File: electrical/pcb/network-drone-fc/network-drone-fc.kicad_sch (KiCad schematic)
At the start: 78 parts, among them J1 U.FL-R-SMT-1, J2 TYPE-C 16PIN 2MD, J3 U.FL GPS, J4 ESC, J5 I2C port, J7 Charging board, U1 ESP32-S3FN8, U2 USBLC6-2SC6, U3 AP63205WU-7, U4 TLV75733PDBVR, U5 TPS7A2033PDBVR, U6 ICM-42688-P, U7 BMP581, U8 MAX-M10S, X1 Q22FA12800101

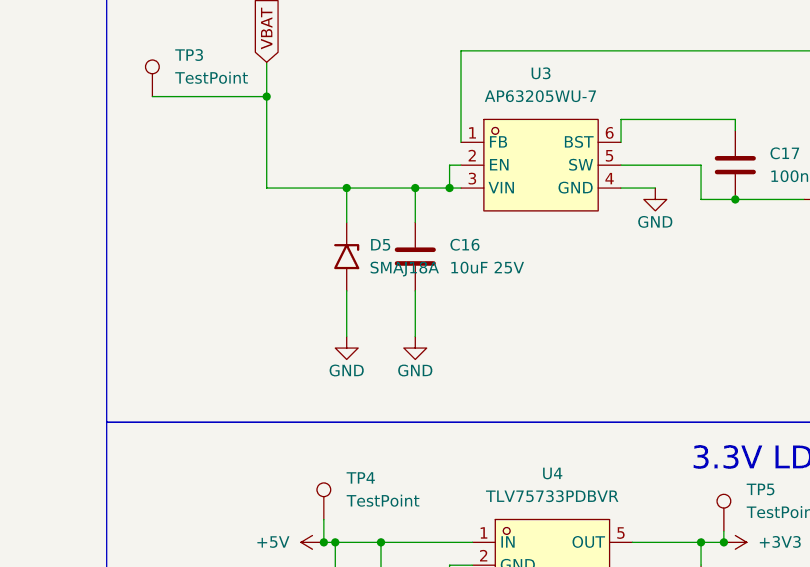
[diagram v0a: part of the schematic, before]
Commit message: Schematic: C35, 100 uF 25 V polymer tantalum bulk capacitor on VBAT
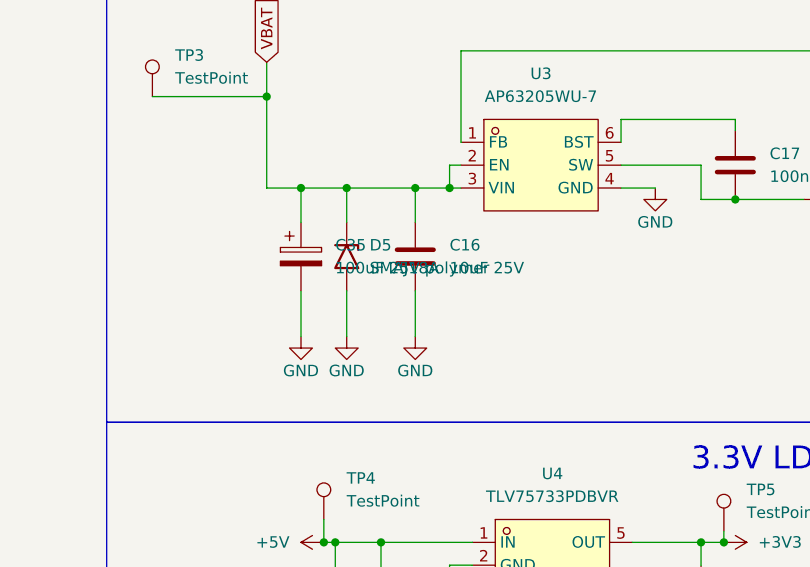
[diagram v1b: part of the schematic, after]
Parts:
- added C35: 100uF 25V polymer, Capacitor_Tantalum_SMD:CP_EIA-7343-31_Kemet-D_HandSolder, symbol Device:C_Polarized
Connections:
- net GND: now also C35.2
- net VBAT: now also C35.1
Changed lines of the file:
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@@
 	(wire
 		(pts
+			(xy 124.46 39.37) (xy 124.46 43.18)
+		)
+		(stroke
+			(width 0)
+			(type default)
+		)
+	)
+	(wire
+		(pts
+			(xy 124.46 50.8) (xy 124.46 55.88)
+		)
+		(stroke
+			(width 0)
+			(type default)
+		)
+	)
+	(junction
+		(at 124.46 39.37)
+		(diameter 0)
+		(color 0 0 0 0)
+	)
+	(wire
+		(pts
 			(xy 278.13 128.27) (xy 280.67 128.27)
 		)
@@
 	(symbol
 		(lib_id "power:GND")
+		(at 124.46 55.88 0)
+		(unit 1)
+		(exclude_from_sim no)
+		(in_bom yes)
+		(on_board yes)
+		(dnp no)
+		(fields_autoplaced yes)
+		(property "Reference" "#PWR0135"
+			(at 124.46 62.23 0)
+			(effects
+				(font
+					(size 1.27 1.27)
+				)
+				(hide yes)
+			)
+		)
+		(property "Value" "GND"
+			(at 124.46 59.69 0)
+			(effects
+				(font
+					(size 1.27 1.27)
+				)
+			)
+		)
+		(property "Footprint" ""
+			(at 124.46 55.88 0)
+			(effects
+				(font
+					(size 1.27 1.27)
+				)
+				(hide yes)
+			)
+		)
+		(property "Datasheet" ""
+			(at 124.46 55.88 0)
+			(effects
+				(font
+					(size 1.27 1.27)
+				)
+				(hide yes)
+			)
+		)
+		(property "Description" "Power symbol creates a global label with name \"GND\" , ground"
+			(at 124.46 55.88 0)
+			(effects
+				(font
+					(size 1.27 1.27)
+				)
+				(hide yes)
+			)
+		)
+		(pin "1"
+		)
+		(instances
+			(project "network-drone-fc"
+				(path "/f9d16c76-ade1-4aab-9e3b-738e650d90d6"
+					(reference "#PWR0135")
+					(unit 1)
+				)
+			)
+		)
+	)
+	(symbol
+		(lib_id "power:GND")
 		(at 191.77 58.42 0)
 		(unit 1)
@@
 					(unit 1)
 				)
+			)
+		)
+	)
+	(symbol
+		(lib_id "Device:C_Polarized")
+		(at 124.46 46.99 0)
+		(unit 1)
+		(exclude_from_sim no)
+		(in_bom yes)
+		(on_board yes)
+		(dnp no)
+		(fields_autoplaced yes)
+		(property "Reference" "C35"
+			(at 128.27 45.7199 0)
+			(effects
+				(font
+					(size 1.27 1.27)
+				)
+				(justify left)
+			)
+		)
+		(property "Value" "100uF 25V polymer"
+			(at 128.27 48.2599 0)
+			(effects
+				(font
+					(size 1.27 1.27)
+				)
+				(justify left)
+			)
+		)
+		(property "Footprint" "Capacitor_Tantalum_SMD:CP_EIA-7343-31_Kemet-D_HandSolder"
+			(at 125.425 50.8 0)
+			(effects
+				(font
+					(size 1.27 1.27)
+				)
+				(hide yes)
+			)
+		)
+		(property "Datasheet" "~"
+			(at 124.46 46.99 0)
+			(effects
+				(font
+					(size 1.27 1.27)
+				)
+				(hide yes)
+			)
+		)
+		(property "Description" "Polarized capacitor, Kyocera AVX TCJD107M025R0055E, LCSC C2159920"
+			(at 124.46 46.99 0)
+			(effects
+				(font
+					(size 1.27 1.27)
+				)
+				(hide yes)
+			)
+		)
+		(pin "2"
+		)
+		(pin "1"
+		)
+		(instances
+			(project "network-drone-fc"
+				(path "/f9d16c76-ade1-4aab-9e3b-738e650d90d6"
+					(reference "C35")
+					(unit 1)
+				)

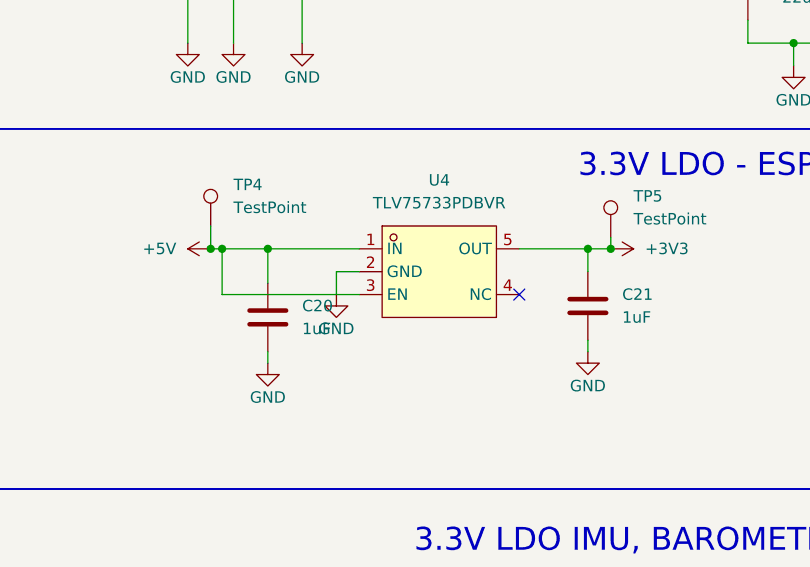
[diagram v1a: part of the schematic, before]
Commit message: Schematic: U4 to TLV75733PDRVR (WSON-6 with thermal pad); C16 to 1206
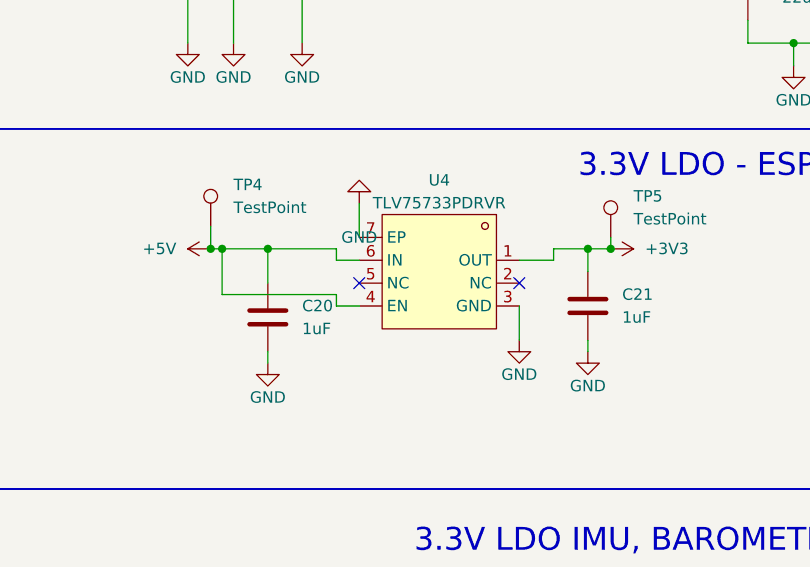
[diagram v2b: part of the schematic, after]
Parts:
- U4: value TLV75733PDBVR -> TLV75733PDRVR; footprint tar_fc:SOT-23-5_L2.9-W1.6-P0.95-LS2.8-BL -> tar_fc:TDFN-6_L2.0-W2.0-P0.65-TL-EP; symbol tar_fc:TLV75733PDBVR -> tar_fc:TLV75733PDRVR; MPN TLV75733PDBVR -> TLV75733PDRVR
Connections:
- net +3V3: now also U4.1 (OUT); no longer U4.5 (OUT)
- net +5V: now also U4.4 (EN), U4.6 (IN); no longer U4.1 (IN), U4.3 (EN)
- net GND: now also U4.3 (GND), U4.7 (EP); no longer U4.2 (GND)
- no-connect marks 45 -> 46
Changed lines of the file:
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@@
 	)
 	(no_connect
-		(at 161.29 83.82)
-	)
-	(no_connect
 		(at 326.39 110.49)
 	)
@@
 	(wire
 		(pts
+			(xy 133.35 78.74) (xy 140.97 78.74)
+		)
+		(stroke
+			(width 0)
+			(type default)
+		)
+	)
+	(wire
+		(pts
+			(xy 140.97 78.74) (xy 140.97 80.01)
+		)
+		(stroke
+			(width 0)
+			(type default)
+		)
+	)
+	(wire
+		(pts
+			(xy 140.97 80.01) (xy 143.51 80.01)
+		)
+		(stroke
+			(width 0)
+			(type default)
+		)
+	)
+	(wire
+		(pts
+			(xy 128.27 83.82) (xy 140.97 83.82)
+		)
+		(stroke
+			(width 0)
+			(type default)
+		)
+	)
+	(wire
+		(pts
+			(xy 140.97 83.82) (xy 140.97 85.09)
+		)
+		(stroke
+			(width 0)
+			(type default)
+		)
+	)
+	(wire
+		(pts
+			(xy 140.97 85.09) (xy 143.51 85.09)
+		)
+		(stroke
+			(width 0)
+			(type default)
+		)
+	)
+	(wire
+		(pts
+			(xy 161.29 80.01) (xy 165.1 80.01)
+		)
+		(stroke
+			(width 0)
+			(type default)
+		)
+	)
+	(wire
+		(pts
+			(xy 165.1 80.01) (xy 165.1 78.74)
+		)
+		(stroke
+			(width 0)
+			(type default)
+		)
+	)
+	(wire
+		(pts
+			(xy 165.1 78.74) (xy 168.91 78.74)
+		)
+		(stroke
+			(width 0)
+			(type default)
+		)
+	)
+	(wire
+		(pts
+			(xy 161.29 85.09) (xy 161.29 88.9)
+		)
+		(stroke
+			(width 0)
+			(type default)
+		)
+	)
+	(wire
+		(pts
+			(xy 143.51 77.47) (xy 143.51 73.66)
+		)
+		(stroke
+			(width 0)
+			(type default)
+		)
+	)
+	(no_connect
+		(at 161.29 82.55)
+	)
+	(no_connect
+		(at 143.51 82.55)
+	)
+	(wire
+		(pts
 			(xy 124.46 39.37) (xy 124.46 43.18)
 		)
@@
 	(wire
 		(pts
-			(xy 133.35 78.74) (xy 143.51 78.74)
-		)
-		(stroke
-			(width 0)
-			(type default)
-		)
-	)
-	(wire
-		(pts
 			(xy 222.25 125.73) (xy 222.25 121.92)
 		)
@@
 	(wire
 		(pts
-			(xy 140.97 81.28) (xy 140.97 83.82)
-		)
-		(stroke
-			(width 0)
-			(type default)
-		)
-	)
-	(wire
-		(pts
 			(xy 137.16 50.8) (xy 137.16 55.88)
 		)
@@
 	(wire
 		(pts
-			(xy 128.27 83.82) (xy 143.51 83.82)
-		)
-		(stroke
-			(width 0)
-			(type default)
-		)
-	)
-	(wire
-		(pts
 			(xy 241.3 106.68) (xy 241.3 110.49)
 		)
@@
 	(wire
 		(pts
-			(xy 161.29 78.74) (xy 168.91 78.74)
-		)
-		(stroke
-			(width 0)
-			(type default)
-		)
-	)
-	(wire
-		(pts
 			(xy 129.54 125.73) (xy 129.54 128.27)
 		)
@@
 		)
 	)
-	(wire
-		(pts
-			(xy 143.51 81.28) (xy 140.97 81.28)
-		)
-		(stroke
-			(width 0)
-			(type default)
-		)
-	)
 	(global_label "ICM_CS"
 		(shape input)
@@
 	)
 	(symbol
-		(lib_id "tar_fc:TLV75733PDBVR")
+		(lib_id "tar_fc:TLV75733PDRVR")
 		(at 152.4 81.28 0)
+		(mirror y)
 		(unit 1)
 		(exclude_from_sim no)
@@
 			)
 		)
-		(property "Value" "TLV75733PDBVR"
+		(property "Value" "TLV75733PDRVR"
 			(at 152.4 73.66 0)
 			(effects
@@
 			)
 		)
-		(property "Footprint" "tar_fc:SOT-23-5_L2.9-W1.6-P0.95-LS2.8-BL"
+		(property "Footprint" "tar_fc:TDFN-6_L2.0-W2.0-P0.65-TL-EP"
 			(at 152.4 91.44 0)
 			(effects
@@
 			)
 		)
-		(property "MPN" "TLV75733PDBVR"
+		(property "MPN" "TLV75733PDRVR"
 			(at 152.4 99.06 0)
 			(effects
@@
 			)
 		)
-		(pin "3"
-		)
 		(pin "1"
 		)
 		(pin "2"
 		)
+		(pin "3"
+		)
 		(pin "4"
 		)
 		(pin "5"
 		)
+		(pin "6"
+		)
+		(pin "7"
+		)
 		(instances
 			(project ""
@@
 	(symbol
 		(lib_id "power:GND")
-		(at 140.97 83.82 0)
+		(at 161.29 88.9 0)
+		(unit 1)
+		(exclude_from_sim no)
+		(in_bom yes)
+		(on_board yes)
+		(dnp no)
+		(fields_autoplaced yes)
+		(property "Reference" "#PWR0136"
+			(at 161.29 95.25 0)
+			(effects
+				(font
+					(size 1.27 1.27)
+				)
+				(hide yes)
+			)
+		)
+		(property "Value" "GND"
+			(at 161.29 92.71 0)
+			(effects
+				(font
+					(size 1.27 1.27)
+				)
+			)
+		)
+		(property "Footprint" ""
+			(at 161.29 88.9 0)
+			(effects
+				(font
+					(size 1.27 1.27)
+				)
+				(hide yes)
+			)
+		)
+		(property "Datasheet" ""
+			(at 161.29 88.9 0)
+			(effects
+				(font
+					(size 1.27 1.27)
+				)
+				(hide yes)
+			)
+		)
+		(property "Description" "Power symbol creates a global label with name \"GND\" , ground"
+			(at 161.29 88.9 0)
+			(effects
+				(font
+					(size 1.27 1.27)
+				)
+				(hide yes)
+			)
+		)
+		(pin "1"
+		)
+		(instances
+			(project "network-drone-fc"
+				(path "/f9d16c76-ade1-4aab-9e3b-738e650d90d6"
+					(reference "#PWR0136")
+					(unit 1)
+				)
+			)
+		)
+	)
+	(symbol
+		(lib_id "power:GND")
+		(at 143.51 73.66 180)
 		(unit 1)
 		(exclude_from_sim no)
@@
 		(dnp no)
 		(fields_autoplaced yes)
-		(property "Reference" "#PWR018"
-			(at 140.97 90.17 0)
+		(property "Reference" "#PWR0137"
+			(at 143.51 80.01 0)
 			(effects
 				(font
@@
 		)
 		(property "Value" "GND"
-			(at 140.97 87.63 0)
+			(at 143.51 77.47 0)
 			(effects
 				(font
@@
 		)
 		(property "Footprint" ""
-			(at 140.97 83.82 0)
+			(at 143.51 73.66 180)
 			(effects
 				(font
@@
 		)
 		(property "Datasheet" ""
-			(at 140.97 83.82 0)
+			(at 143.51 73.66 180)
 			(effects
 				(font
@@
 		)
 		(property "Description" "Power symbol creates a global label with name \"GND\" , ground"
-			(at 140.97 83.82 0)
+			(at 143.51 73.66 180)
 			(effects
 				(font
@@
 			(project "network-drone-fc"
 				(path "/f9d16c76-ade1-4aab-9e3b-738e650d90d6"
-					(reference "#PWR018")
+					(reference "#PWR0137")
 					(unit 1)
 				)
